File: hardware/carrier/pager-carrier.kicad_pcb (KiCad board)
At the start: 2 copper layers, 62.8 x 46 mm, 92 parts, among them J1 PANEL, J2 CARDKB, J3 HAPTIC, J4 EXT_LED, J5 PIEZ, J6 USB4235, J7 BATTERY, M1 Walter, Q1 UMH3N, Q2 SI1308EDL, Q3 MMST3904, Q4 AO3401A, SW1 SKQGAFE010, SW2 JS102011SAQN, U1 CP2102N-A02-GQFN24, U2 SN74LVC2G126DCUR, U3 DRV2605LDGSR, U4 LIS2DW12TR, U5 BQ25185DLHR, U6 MAX17048G+T10, U7 TPS62840DLCR

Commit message: Replace JP1 with 0402 0R link, shrink SW1/SW2 to KMR2 and MSK12C02
JP1 (solder jumper) becomes R39, a fitted 0402 0R on the auto-boot line:
pull it to disable auto boot. SW1 is now a C&K KMR221GLFS (4.2 x 2.8 x
1.3 mm, C72443) and SW2 a Shou Han MSK12C02 top-knob slide switch
(C431540). Footprints swapped in the PCB with nets preserved (SW1 pads
now carry FL_BTN/GND). Adds the JLCPCB design rules file.

Co-Authored-By: Claude Fable 5.1 <noreply@anthropic.com>
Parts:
- removed JP1: auto-boot, Jumper:SolderJumper-2_P1.3mm_Bridged_RoundedPad1.0x1.5mm
- added R39: 0R, Resistor_SMD:R_0402_1005Metric, F.Cu at (91.8, 68.7)
- SW1: value SKQGAFE010 -> KMR221GLFS; footprint Button_Switch_SMD:SW_SPST_SKQG_WithoutStem -> Button_Switch_SMD:SW_Push_1P1T_NO_CK_KMR2
- SW2: value JS102011SAQN -> MSK12C02; footprint Button_Switch_SMD:SW_SPDT_CK_JS102011SAQN -> Button_Switch_SMD:SW_SPDT_Shouhan_MSK12C02
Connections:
- SW1 pad 1: (no net) -> /Core/FL_BTN
- SW1 pad 2: (no net) -> GND

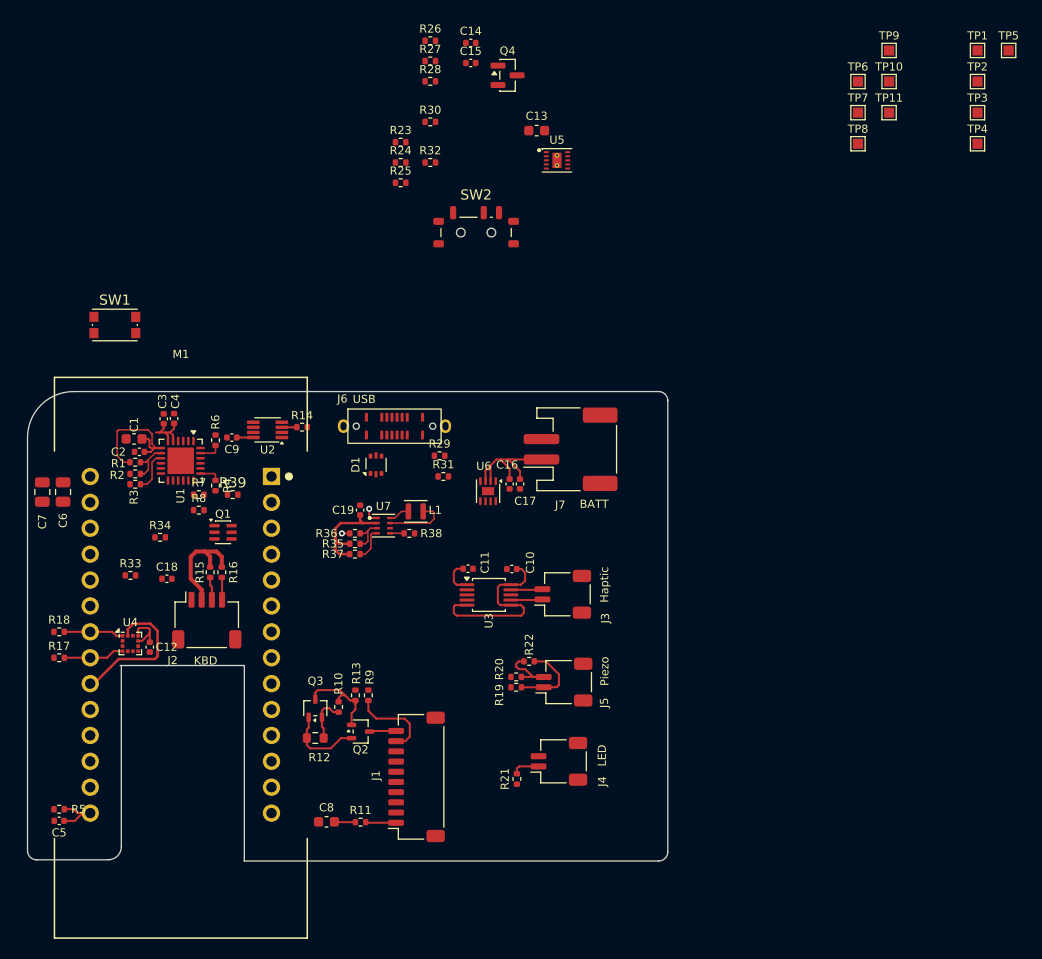
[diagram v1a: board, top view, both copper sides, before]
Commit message: Carrier board v0.1: fully routed, DRC clean against JLCPCB rules
Fable cleaned up the initial hand-placed design: closed the outline,
placed the switches, charger and remaining passives, routed every net
(GND as pours plus stitching vias) and brought the board to zero DRC
errors against pager-carrier.kicad_dru. Only the parked test points
remain unconnected.

Co-Authored-By: Claude Fable 5.1 <noreply@anthropic.com>
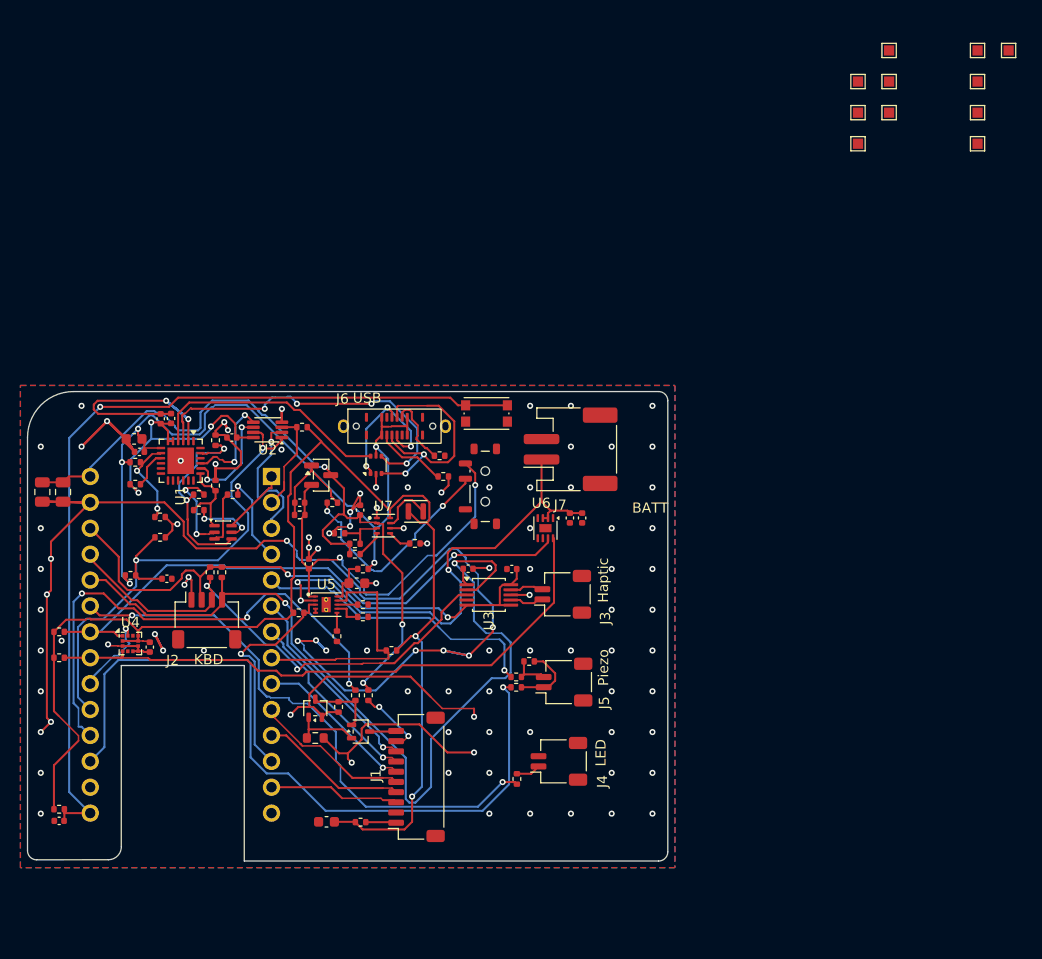
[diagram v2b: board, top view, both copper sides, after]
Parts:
- moved R26 59.9 mm to (107.4, 84.0), turned to 180 degrees
- moved R27 53.7 mm to (104.6, 79.5)
- moved R28 53.7 mm to (98.3, 80.3)
- moved C15 51.6 mm to (99.3, 75.5), turned to 90 degrees
- moved U5 49.1 mm to (101.0, 79.5)
- moved C14 48.1 mm to (98.4, 69.5)
- moved C13 47.8 mm to (104.0, 77.4)
- moved R24 46.9 mm to (102.0, 82.6), turned to -90 degrees
- moved Q4 43.3 mm to (100.5, 66.8)
- moved R25 42.7 mm to (104.6, 80.7)
- moved R23 42.0 mm to (104.6, 76.0), turned to 180 degrees
- moved R30 38.6 mm to (101.6, 69.5)
- moved SW1 37.5 mm to (116.7, 60.8)
- moved R32 36.9 mm to (98.4, 70.7)
- moved SW2 24.9 mm to (116.6, 67.9), turned to 90 degrees
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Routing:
- net GND: track 6.99 -> 339.2 mm, vias 2 -> 103
- net 3V3: track 8.89 -> 130.1 mm, vias 0 -> 2
- net /Core/AWK_SCL: track 2.20 -> 88.9 mm, vias 0 -> 2
- net /Core/FL_BTN: track 5.58 -> 86.3 mm, vias 0 -> 1
- net /Core/PIEZ_P: track 0.00 -> 72.5 mm, vias 0 -> 1
- net SYS_SW: track 10.4 -> 73.3 mm, vias 0 -> 3
- net VBUS: track 13.0 -> 75.5 mm, vias 0 -> 5
- net /Core/EXT_LED: track 0.00 -> 55.4 mm, vias 0 -> 2
- net AON_SDA: track 5.98 -> 58.8 mm
- net VBUS_DET: track 0.00 -> 52.8 mm, vias 0 -> 2
- net AON_SCL: track 5.88 -> 57.9 mm, vias 0 -> 1
- net /Core/FL_PWM: track 0.00 -> 50.0 mm, vias 0 -> 3
- net /Core/AWK_SDA: track 2.57 -> 50.3 mm, vias 0 -> 2
- net SYS: track 0.00 -> 40.0 mm, vias 0 -> 2
- net VBAT: track 13.3 -> 49.3 mm, vias 0 -> 3
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- added copper zone on B.Cu, net GND
- added copper zone on F.Cu, net GND
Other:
- outline, holes or cut-outs redrawn

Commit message: Carrier v0.2c WIP: 2-layer re-layout, full Walter width, headers on the right edge
Work in progress, not DRC-complete. The board is re-laid out on the real tin
geometry measured from the owner's assembly STEP (inner corner R13.2 at
(81.69, 69.35); walls y 56.1/113.3) instead of the estimated R19 arc:

- Outline x 74.3..115, y 57.4..108.4, stepped at the WiFi keepout line (106.3)
  over the Walter; SIM notch replaced by a 2 mm pin-eject hole at (86.25, 93.2).
- All six cable headers face +X on the right edge (J2, J1, J7, J3, J4, J5).
- USB bridge (U1/U2), auto-reset cluster and BRG_3V3 caps on the bottom
  inside the Walter shadow; U2 below U1 so its TXD/RXD pads face U1's.
- Hand-routed 2-layer USB-C corner (D+ tie as a short top diagonal, D- tie on
  the bottom), BQ25185 escapes, BRG_3V3 into U1, ESD-diode ground via.
- Freerouting output (variant 9) with ground pours; 0 DRC errors, parity OK.
  Open: SYS_SW (whole net, blocked by the ground via above U7 pin 1), nine
  short local links, three ground islands; test points stay parked.
- GCT USB4235 vertical USB-C: real STEP model (rotate -90 about X) replaces
  the placeholder box in the footprint and the board.
- HANDOFF-v0.2.md: v0.2c addendum with owner decisions, tin geometry, pipeline
  state, root causes of the wasted runs and what is left to finish by hand.

Co-Authored-By: Claude Fable 5.1 <noreply@anthropic.com>
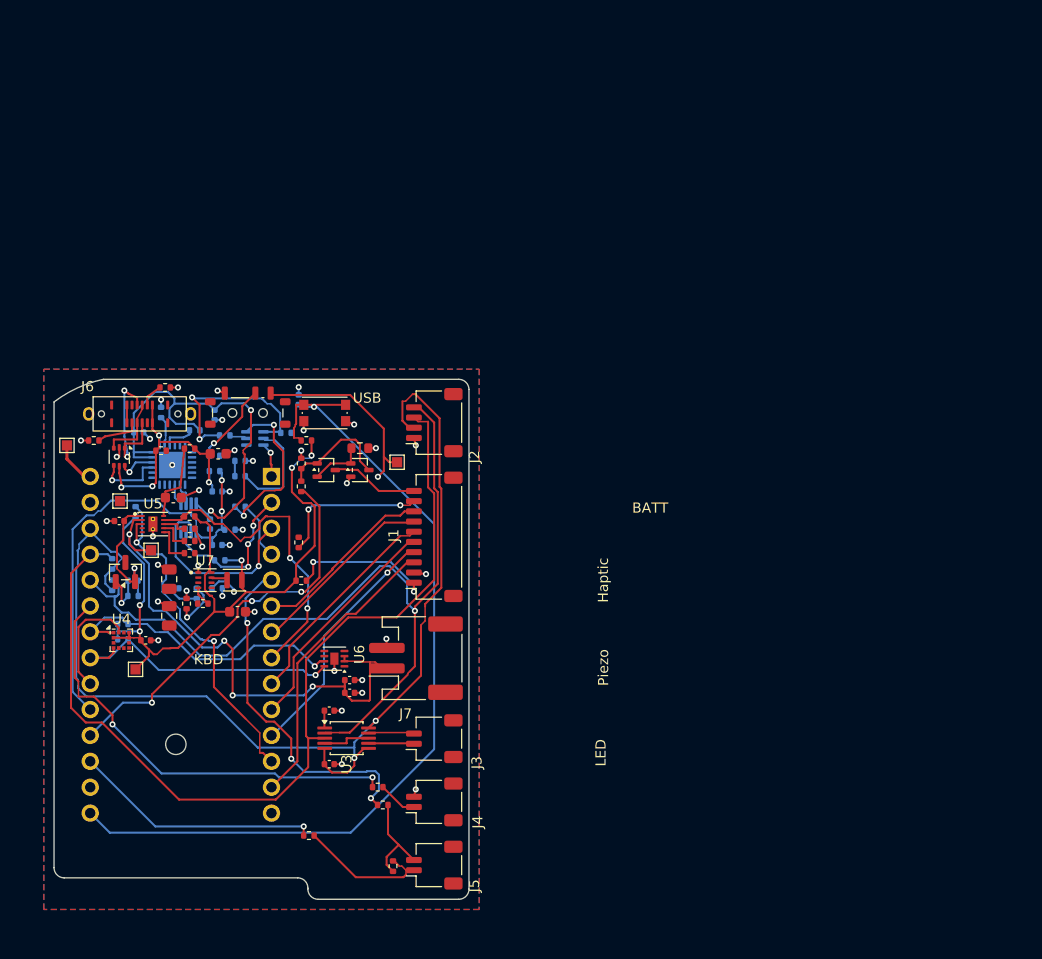
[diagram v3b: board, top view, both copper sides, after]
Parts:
- removed TP1: AWK_EN_N, TestPoint:TestPoint_Pad_1.0x1.0mm
- removed TP2: TP_IO1, TestPoint:TestPoint_Pad_1.0x1.0mm
- removed TP3: TP_IO5, TestPoint:TestPoint_Pad_1.0x1.0mm
- removed TP4: FL_BTN, TestPoint:TestPoint_Pad_1.0x1.0mm
- removed TP5: 3V3_AWK, TestPoint:TestPoint_Pad_1.0x1.0mm
- removed TP6: GND, TestPoint:TestPoint_Pad_1.0x1.0mm
- C14, C18, C19, C2, C3, C4, C5, C9, Q1, R14, R15, R16, R17, R18, R2, R28, R3, R30, R32, R33, R34, R35, R38, R39, R4, R6, R7, R8, U1, U2: moved to B.Cu
- moved TP11 91.9 mm to (82.3, 85.9)
- moved TP9 89.5 mm to (75.6, 63.9)
- moved TP10 85.8 mm to (83.8, 74.2)
- moved TP7 81.8 mm to (80.8, 69.3)
- moved TP8 55.0 mm to (108.0, 65.5)
- moved C5 47.5 mm to (98.3, 59.4), turned to 90 degrees
- moved R5 43.5 mm to (99.0, 63.4), turned to 0 degrees
- moved R31 34.5 mm to (78.2, 63.4), turned to 180 degrees
- moved J2 29.6 mm to (111.6, 61.6), turned to 90 degrees
- moved R12 28.8 mm to (104.3, 64.2)
- moved C17 28.5 mm to (103.3, 88.2), turned to 0 degrees
- moved R29 27.7 mm to (85.2, 58.2)
- moved C16 26.8 mm to (103.3, 86.9), turned to 0 degrees
- moved C10 26.2 mm to (101.3, 95.2), turned to 0 degrees
- moved Q2 25.9 mm to (101.0, 66.3)
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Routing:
- net GND: track 339.2 -> 39.1 mm, vias 103 -> 39
- net SYS_SW: track 73.3 -> 7.48 mm, vias 3 -> 0
- net 3V3: track 130.1 -> 75.5 mm, vias 2 -> 5
- net 3V3_AWK: track 56.4 -> 108.2 mm
- net VBUS: track 75.5 -> 26.9 mm, vias 5 -> 4
- net /Core/PIEZ_P: track 72.5 -> 24.5 mm
- net /Core/AWK_SDA: track 50.3 -> 91.9 mm, vias 2 -> 0
- net AON_SDA: track 58.8 -> 28.5 mm, vias 0 -> 1
- net AON_SCL: track 57.9 -> 29.3 mm
- net USB_DP: track 34.8 -> 6.69 mm, vias 4 -> 1
- net USB_DM: track 24.2 -> 3.69 mm, vias 0 -> 1
- net Net-(D1-I/O2-Pad3): track 23.6 -> 6.65 mm, vias 2 -> 0
- net /Core/BRG_3V3: track 26.5 -> 43.0 mm, vias 3 -> 2
- net /Core/EINK_SCK: track 12.8 -> 28.7 mm
- net Net-(SW2-B): track 22.2 -> 8.12 mm, vias 2 -> 1
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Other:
- board size 62.8 x 46 mm -> 40.7 x 51 mm

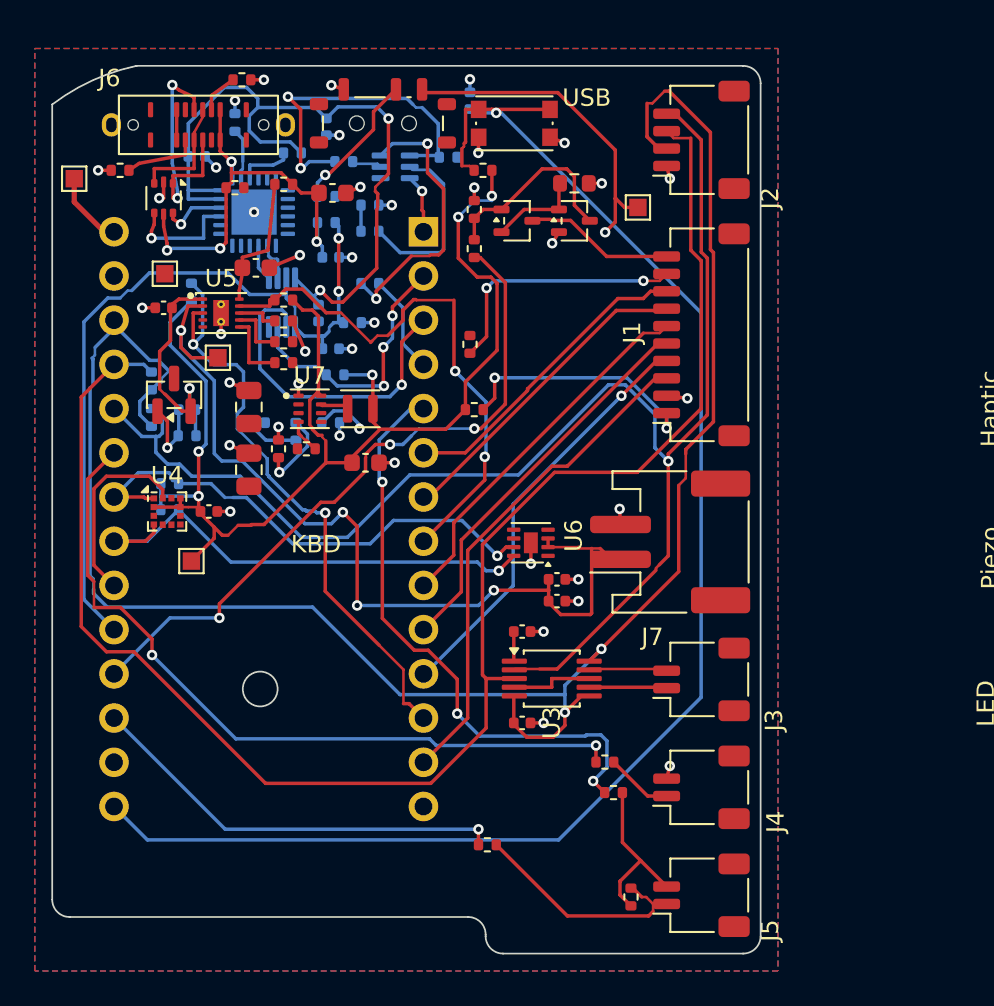
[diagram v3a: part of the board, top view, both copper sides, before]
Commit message: Carrier v0.2c WIP: cassette screw holes, top-actuated SW2, wider board, panel schematic fixes
Work in progress for the 3D-printed display cassette; routing is DRC-clean
(0 errors) with 14 signal links and 3 ground islands left for hand finishing
(list in HANDOFF-v0.2.md).

Carrier:
- H1-H3 M2 cassette screw holes (2.2 mm NPTH, 4.5 mm copper-free annulus on
  both layers via footprint rule areas + per-hole DRC rules) at (77.4, 60.9),
  (111.2, 59.95), (111.2, 105.85); schematic symbols in the core sheet.
- SW2 power switch -> C&K JS102011SAQN top-actuated SPDT (LCSC C221660),
  travel along X; top strip is now J6, SW1, SW2 (x 80.0..108.5).
- Board widened to x 120.5 so the right-side holes fit beside the header
  column (J2 keyboard header stays topmost, cable into the plate channel).
- F.Fab note to trim the Walter header pins flush; stale KBD label moved.
- 3D models added: JS102011SAQN, MAX17048 (U6), JST PH S2B-PH-SM4-TB (J7);
  STEP export in out/ for the Fusion assembly.
- Owner's manual schematic edits (test points) included.

Panel:
- Owner's rearranged panel_main.kicad_sch with the EPD_GDR wire gap closed
  (J1 pin 2 back on the boost gate net); both front-light FPC connectors kept.

Co-Authored-By: Claude Fable 5.1 <noreply@anthropic.com>
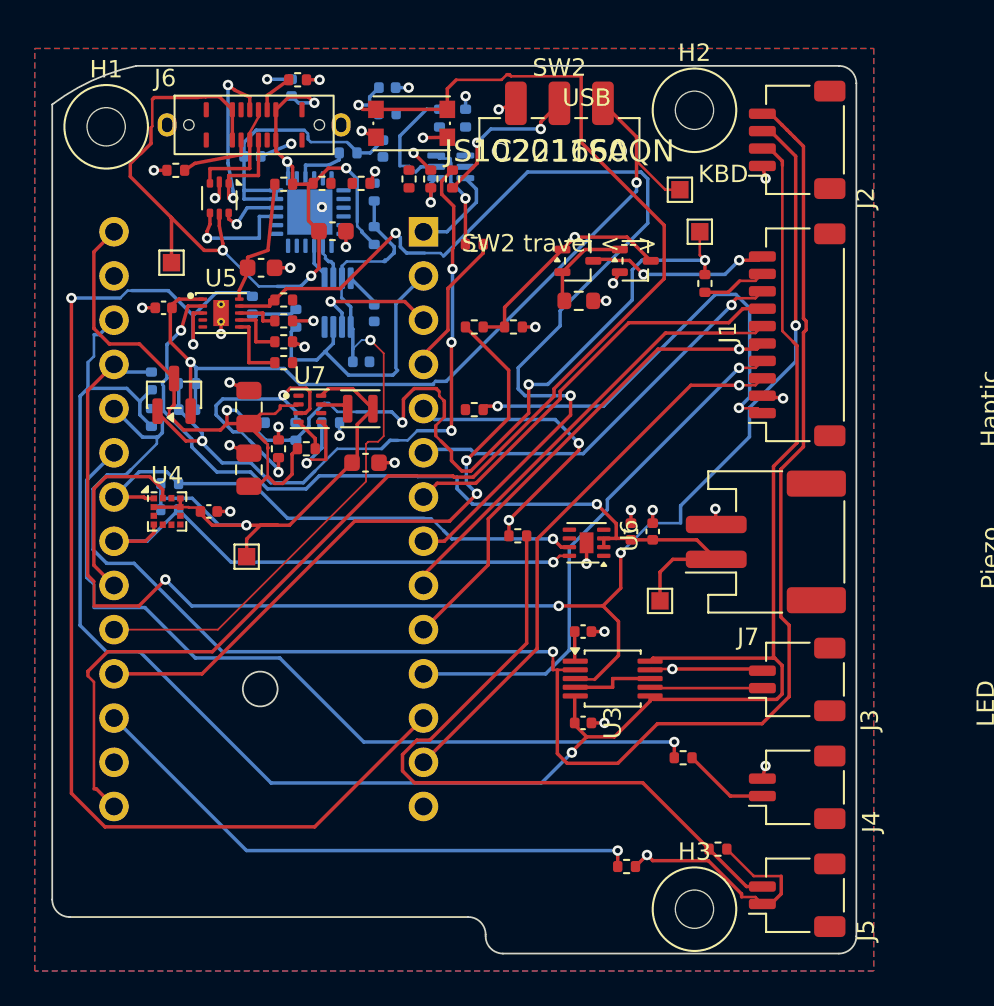
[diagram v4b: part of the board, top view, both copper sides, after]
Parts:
- added H1: Cassette M2, pager-carrier:MountingHole_2.2mm_M2_Cassette, F.Cu at (77.4, 60.9)
- added H2: Cassette M2, pager-carrier:MountingHole_2.2mm_M2_Cassette, F.Cu at (111.2, 60.0)
- added H3: Cassette M2, pager-carrier:MountingHole_2.2mm_M2_Cassette, F.Cu at (111.2, 105.8)
- R2, R30, R39, R4, R8: moved to F.Cu
- R5: moved to B.Cu
- SW2: value MSK12C02 -> JS102011SAQN; footprint Button_Switch_SMD:SW_SPDT_Shouhan_MSK12C02 -> Button_Switch_SMD:SW_SPDT_CK_JS102011SAQN
- moved TP9 36.1 mm to (111.5, 66.9)
- moved TP10 29.0 mm to (109.2, 88.1)
- moved R20 15.7 mm to (101.0, 84.4)
- moved R13 13.9 mm to (111.8, 69.9)
- moved SW2 10.3 mm to (103.4, 62.3)
- moved C2 10.0 mm to (88.0, 58.6), turned to 90 degrees
- moved R19 8.10 mm to (107.3, 103.4)
- moved R2 8.05 mm to (92.0, 64.2), turned to 0 degrees
- moved R34 7.60 mm to (92.8, 64.7), turned to 90 degrees
- moved R30 7.32 mm to (97.3, 63.9), turned to 90 degrees
- moved R10 7.12 mm to (100.8, 72.4), turned to 0 degrees
- moved C17 6.80 mm to (108.8, 84.2), turned to 90 degrees
- moved R12 6.75 mm to (104.5, 70.9)
- moved R39 6.41 mm to (98.5, 67.7)
- moved R5 6.39 mm to (93.5, 60.1)
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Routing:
- net SYS_SW: track 7.48 -> 77.0 mm, vias 0 -> 4
- net 3V3: track 75.5 -> 34.0 mm, vias 5 -> 1
- net Net-(Q4-G): track 4.80 -> 39.4 mm, vias 1 -> 4
- net CHG_STAT2: track 35.2 -> 67.9 mm
- net Net-(J5-Pin_2): track 9.81 -> 40.3 mm
- net CHG_STAT1: track 31.7 -> 59.3 mm
- net VBUS: track 26.9 -> 53.8 mm, vias 4 -> 5
- net /Core/BRG_3V3: track 43.0 -> 18.8 mm, vias 2 -> 0
- net Net-(Q1B-E2): track 19.4 -> 0.00 mm, vias 2 -> 0
- net SYS: track 32.6 -> 50.8 mm
- net /Core/PIEZ_N: track 34.2 -> 16.7 mm, vias 3 -> 2
- net /Core/AWK_SCL: track 83.4 -> 100.6 mm
- net /Core/3V3_J1: track 14.4 -> 25.8 mm
- net /Core/ESP_TX0: track 18.9 -> 7.50 mm
- net /Core/FL_P: track 14.8 -> 3.74 mm, vias 2 -> 0
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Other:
- board size 40.7 x 51 mm -> 46.2 x 51 mm
- board text added: "FAB NOTE: trim the 28 Walter header pins flush with the solder fillets after soldering (untrimmed pins reach 5 mm above this board, into the display glass)"
- board text added: "SW2 travel <-->"
